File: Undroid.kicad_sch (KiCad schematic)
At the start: 43 parts, among them J1 AudioJack2, J2 Conn_01x15

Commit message: pcb-master: Update prototype.
Signed-off-by: Amlal EL Mahrouss <amlalelmahrouss@icloud.com>
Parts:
- removed AE1: Antenna_Shield, RF_Antenna:Texas_SWRA117D_2.4GHz_Right, symbol Device:Antenna_Shield
- removed ANT_S1, SD_S1, SIM_S1, USB_S1: RFShield_OnePiece, RF_Shielding:Laird_Technologies_97-2002_25.40x25.40mm, symbol Device:RFShield_OnePiece
- added ANT1: Antenna, RF_Antenna:NiceRF_SW868-TH13_868Mhz, symbol Device:Antenna
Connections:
- net at SIM_CHIP1.32 (ANT): now also ANT1.1 (A)
- no-connect marks 114 -> 117

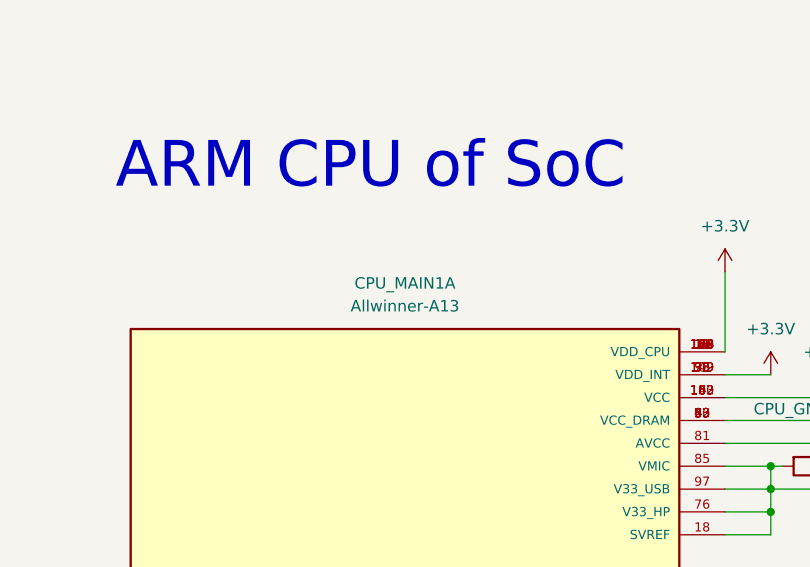
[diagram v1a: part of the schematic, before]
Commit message: pcb-master: Fix schematic and PCB.
Signed-off-by: Amlal EL Mahrouss <amlalelmahrouss@icloud.com>
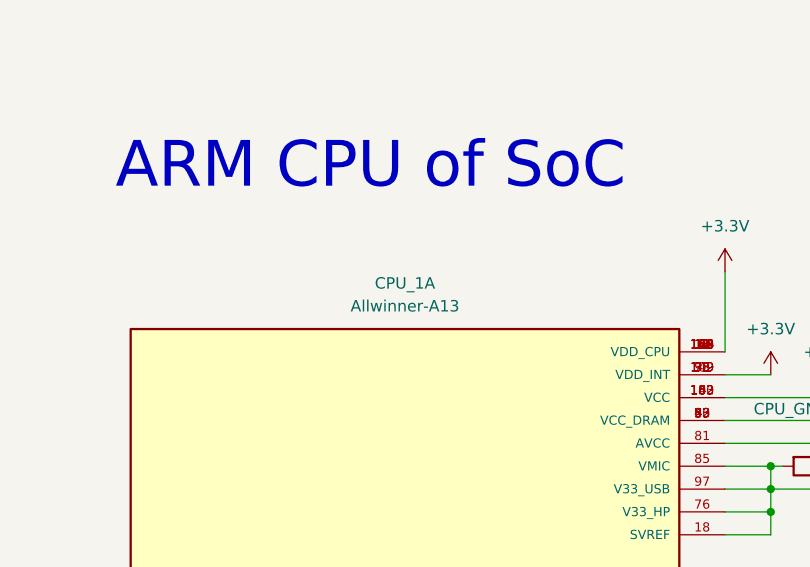
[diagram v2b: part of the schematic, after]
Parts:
- renumbered CPU_MAIN1 to CPU_1
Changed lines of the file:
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@@
 		(dnp no)
 		(fields_autoplaced yes)
-		(property "Reference" "CPU_MAIN1"
+		(property "Reference" "CPU_1"
 			(at 508 81.28 0)
 			(effects
@@
 			(project "Undroid"
 				(path "/5d3a3bfa-72d2-42b8-bac3-6ac6fe44d852"
-					(reference "CPU_MAIN1")
+					(reference "CPU_1")
 					(unit 1)
 				)

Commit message: pcb-master: update schematic.
Signed-off-by: Amlal EL Mahrouss <amlalelmahrouss@icloud.com>
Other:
- note added: "CONN 1x15"
- note removed: "The board also contains EMI shields. for Antennas, SIM, SD, Power..."
- moved on the sheet: J2
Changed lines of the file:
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@@
 	(title_block
 		(title "Motherboard")
-		(date "2024-06-17")
-		(rev "8")
+		(date "2024-06-19")
+		(rev "9")
 		(company "Zeta")
 	)
@@
 	)
 	(no_connect
-		(at 304.8 377.19)
+		(at 242.57 356.87)
 	)
 	(no_connect
@@
 	)
 	(no_connect
-		(at 307.34 377.19)
+		(at 245.11 356.87)
 	)
 	(no_connect
@@
 	)
 	(no_connect
-		(at 312.42 377.19)
+		(at 250.19 356.87)
 	)
 	(no_connect
@@
 	)
 	(no_connect
-		(at 325.12 377.19)
+		(at 262.89 356.87)
 	)
 	(no_connect
@@
 	)
 	(no_connect
-		(at 309.88 377.19)
+		(at 247.65 356.87)
 	)
 	(no_connect
-		(at 327.66 377.19)
+		(at 265.43 356.87)
 	)
 	(no_connect
@@
 	)
 	(no_connect
-		(at 314.96 377.19)
+		(at 252.73 356.87)
 	)
 	(no_connect
@@
 	)
 	(no_connect
-		(at 317.5 377.19)
+		(at 255.27 356.87)
 	)
 	(no_connect
@@
 	)
 	(no_connect
-		(at 322.58 377.19)
+		(at 260.35 356.87)
 	)
 	(no_connect
@@
 	)
 	(no_connect
-		(at 330.2 377.19)
+		(at 267.97 356.87)
 	)
 	(no_connect
@@
 	)
 	(no_connect
-		(at 320.04 377.19)
+		(at 257.81 356.87)
 	)
 	(wire
@@
 		)
 	)
-	(text "The board also contains EMI shields.\nfor Antennas, SIM, SD, Power..."
+	(text "Bridge MCU"
 		(exclude_from_sim yes)
-		(at 92.456 383.286 0)
+		(at 295.402 66.294 0)
 		(effects
 			(font
@@
 		)
 	)
-	(text "Bridge MCU"
+	(text "Memory (SIM, Flash, SD)"
 		(exclude_from_sim yes)
-		(at 295.402 66.294 0)
+		(at 105.156 326.898 0)
 		(effects
 			(font
@@
 		)
 	)
-	(text "Memory (SIM, Flash, SD)"
+	(text "ARM GPU of SoC"
 		(exclude_from_sim yes)
-		(at 79.248 317.754 0)
+		(at 505.206 242.824 0)
 		(effects
 			(font
@@
 		)
 	)
-	(text "ARM GPU of SoC"
+	(text "ARM CPU of SoC"
 		(exclude_from_sim yes)
-		(at 493.522 243.078 0)
+		(at 509.778 61.468 0)
 		(effects
 			(font
@@
 		)
 	)
-	(text "ARM CPU of SoC"
+	(text "Power Line"
 		(exclude_from_sim yes)
-		(at 504.19 68.326 0)
+		(at 177.8 178.054 0)
 		(effects
 			(font
@@
 		)
 	)
-	(text "Power Line"
+	(text "CONN 1x15"
 		(exclude_from_sim yes)
-		(at 212.09 124.968 0)
+		(at 259.842 332.486 0)
 		(effects
 			(font
@@
 	(text "GPRS modem"
 		(exclude_from_sim yes)
-		(at 80.01 47.498 0)
+		(at 73.152 53.848 0)
 		(effects
 			(font
@@
 	(global_label "CONN_NMI_N"
 		(shape input)
-		(at 332.74 377.19 90)
+		(at 270.51 356.87 90)
 		(fields_autoplaced yes)
 		(effects
@@
 		)
 		(property "Intersheetrefs" "${INTERSHEET_REFS}"
-			(at 332.74 362.2909 90)
+			(at 270.51 341.9709 90)
 			(effects
 				(font
@@
 	(global_label "RESET"
 		(shape input)
-		(at 337.82 377.19 90)
+		(at 275.59 356.87 90)
 		(fields_autoplaced yes)
 		(effects
@@
 		)
 		(property "Intersheetrefs" "${INTERSHEET_REFS}"
-			(at 337.82 368.4597 90)
+			(at 275.59 348.1397 90)
 			(effects
 				(font
@@
 	(global_label "RTC_IN"
 		(shape input)
-		(at 335.28 377.19 90)
+		(at 273.05 356.87 90)
 		(fields_autoplaced yes)
 		(effects
@@
 		)
 		(property "Intersheetrefs" "${INTERSHEET_REFS}"
-			(at 335.28 367.7943 90)
+			(at 273.05 347.4743 90)
 			(effects
 				(font
@@
 	(global_label "UBOOT"
 		(shape input)
-		(at 340.36 377.19 90)
+		(at 278.13 356.87 90)
 		(fields_autoplaced yes)
 		(effects
@@
 		)
 		(property "Intersheetrefs" "${INTERSHEET_REFS}"
-			(at 340.36 367.9757 90)
+			(at 278.13 347.6557 90)
 			(effects
 				(font
@@
 	(symbol
 		(lib_id "Connector_Generic:Conn_01x15")
-		(at 322.58 382.27 270)
+		(at 260.35 361.95 270)
 		(unit 1)
 		(exclude_from_sim no)
@@
 		(fields_autoplaced yes)
 		(property "Reference" "J2"
-			(at 322.58 386.08 90)
+			(at 260.35 365.76 90)
 			(effects
 				(font
@@
 		)
 		(property "Value" "Conn_01x15"
-			(at 322.58 388.62 90)
+			(at 260.35 368.3 90)
 			(effects
 				(font
@@
 		)
 		(property "Footprint" "Connector_PinHeader_1.00mm:PinHeader_1x15_P1.00mm_Vertical"
-			(at 322.58 382.27 0)
+			(at 260.35 361.95 0)
 			(effects
 				(font
@@
 		)
 		(property "Datasheet" "~"
-			(at 322.58 382.27 0)
+			(at 260.35 361.95 0)
 			(effects
 				(font
@@
 		)
 		(property "Description" "Generic connector, single row, 01x15, script generated (kicad-library-utils/schlib/autogen/connector/)"
-			(at 322.58 382.27 0)
+			(at 260.35 361.95 0)
 			(effects
 				(font

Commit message: pcb-master: improve schematics to be much more organized.
Signed-off-by: Amlal EL Mahrouss <amlalelmahrouss@icloud.com>
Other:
- title: Motherboard -> Phone motherboard
- moved on the sheet: ANT1, BRIDGE_CHIP1, CC1_R1, CC2_R1, CPU_1A, CPU_GND_CPU1, CPU_GND_USB1, CPU_GND_VDDQ1, CPU_GND_VREFCA1, CPU_GND_VREFQ1, D1, DDR_RAM1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

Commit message: pcb-master: improve schematic and PCB.
Signed-off-by: Amlal EL Mahrouss <amlalelmahrouss@icloud.com>
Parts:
- removed CPU_GND_USB1, CPU_GND_VDDQ1, CPU_GND_VREFCA1, CPU_GND_VREFQ1, RCPU_GND_VDD1: R, Resistor_SMD:R_0201_0603Metric, symbol Device:R
- added C1: C_Polarized, Capacitor_Tantalum_SMD:CP_EIA-2012-12_Kemet-R, symbol Device:C_Polarized
- added MBCI_0: AVR32DB32x-xRXB, Package_DFN_QFN:QFN-32-1EP_5x5mm_P0.5mm_EP3.1x3.1mm, symbol MCU_Microchip_AVR_Dx:AVR32DB32x-xRXB
- added MBCI_NETWORK1, MBCI_VIDEO1: Conn_01x15, Connector_PinHeader_1.00mm:PinHeader_1x15_P1.00mm_Vertical, symbol Connector_Generic:Conn_01x15
- added MBCI_PWR_R1, MCU_PWR_R2, RAM_GND_VSS_R3, RAM_PWR_R2: R, Resistor_SMD:R_0201_0603Metric, symbol Device:R
- renumbered CPU_GND_CPU1 to CPU_GND_1, J1 to JACK_PORT1, J2 to MBCI_IO1, RVCC_FL_2 to VCC_FL_2, RVCC_S_1 to VCC_S_1
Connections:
- net GND: now also MBCI_IO1.15 (Pin_15), MBCI_NETWORK1.15 (Pin_15), MBCI_VIDEO1.15 (Pin_15), RAM_GND_VSS_R3.1
- net RESET: now also MBCI_0.26 (~{RESET}/PF6)
- net VBUS_USBC: now also MCU_PWR_R1.2, R_VDD_3V3.1, VBAT_R1.1, MBCI_PWR_R1.2, MCU_PWR_R2.2
- net CLK: now reaches MBCI_IO1.11 (Pin_11)
- net CLK: now also MBCI_NETWORK1.11 (Pin_11), MBCI_VIDEO1.11 (Pin_11)
- net UBOOT_MBCI: now reaches MBCI_IO1.5 (Pin_5)
- net UBOOT_MBCI: now also MBCI_0.27 (UPDI)
- net 3.3V: now reaches MBCI_IO1.8 (Pin_8)
- net 3.3V: now also MBCI_NETWORK1.8 (Pin_8), MBCI_VIDEO1.8 (Pin_8)
- net at DDR_RAM1.B2 (VDD), DDR_RAM1.D9 (VDD), DDR_RAM1.G7 (VDD)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: now also RAM_PWR_R2.1
- removed net +3.3V: CPU_1.100 (VCC), CPU_1.109 (VDD_INT), CPU_1.11 (VDD_CPU), CPU_1.142 (VCC), CPU_1.149 (VDD_INT), CPU_1.156 (VDD_CPU), CPU_1.16 (VDD_CPU), CPU_1.163 (VCC), CPU_1.164 (VDD_CPU), CPU_1.169 (VDD_CPU), CPU_1.173 (VDD_CPU), CPU_1.23 (VCC_DRAM), CPU_1.30 (VCC_DRAM), CPU_1.35 (VDD_INT), CPU_1.4 (VDD_CPU), CPU_1.43 (VCC_DRAM), CPU_1.5 (VCC), CPU_1.53 (VCC_DRAM), CPU_1.62 (VCC_DRAM), CPU_1.73 (VDD_INT), CPU_1.81 (AVCC), CPU_1.9 (VDD_CPU), CPU_1.98 (VDD_INT), MCU_PWR_R1.2, R_VDD_3V3.1, VBAT_R1.1
- new net: CPU_1.109 (VDD_INT), CPU_1.149 (VDD_INT), CPU_1.35 (VDD_INT), CPU_1.73 (VDD_INT), CPU_1.98 (VDD_INT)
- new net: CPU_1.11 (VDD_CPU), CPU_1.156 (VDD_CPU), CPU_1.16 (VDD_CPU), CPU_1.164 (VDD_CPU), CPU_1.169 (VDD_CPU), CPU_1.173 (VDD_CPU), CPU_1.4 (VDD_CPU), CPU_1.9 (VDD_CPU)
- new net: C1.1, MBCI_0.28 (VDD), MBCI_PWR_R1.1
- new net: C1.2, MBCI_0.29 (GND), MBCI_0.33 (GND), RAM_GND_VSS_R3.2
- new net ALPHA_V: MBCI_0.9 (PC3), MBCI_VIDEO1.4 (Pin_4)
- new net AVAIL_N: MBCI_0.30 (XTALHF1/PA0), MBCI_NETWORK1.6 (Pin_6)
- new net BLUE_V: MBCI_0.22 (PF2), MBCI_VIDEO1.3 (Pin_3)
- new net CPU_PWR: CPU_1.100 (VCC), CPU_1.142 (VCC), CPU_1.163 (VCC), CPU_1.5 (VCC), MCU_PWR_R2.1
- new net DAT0_N: MBCI_0.3 (PA5), MBCI_NETWORK1.1 (Pin_1)
- new net DAT1_N: MBCI_0.2 (PA4), MBCI_NETWORK1.2 (Pin_2)
- new net DAT2_N: MBCI_0.1 (PA3), MBCI_NETWORK1.3 (Pin_3)
- new net DAT3_N: MBCI_0.32 (PA2), MBCI_NETWORK1.4 (Pin_4)
- new net DAT4_N: MBCI_0.31 (XTALHF2/PA1), MBCI_NETWORK1.5 (Pin_5)
- new net DRAM_PWR: CPU_1.23 (VCC_DRAM), CPU_1.30 (VCC_DRAM), CPU_1.43 (VCC_DRAM), CPU_1.53 (VCC_DRAM), CPU_1.62 (VCC_DRAM), RAM_PWR_R2.2
- new net GREEN_V: MBCI_0.21 (XTAL32K2/PF1), MBCI_VIDEO1.2 (Pin_2)
- new net HSYNC_V: MBCI_0.8 (PC2), MBCI_VIDEO1.5 (Pin_5)
- new net RED_V: MBCI_0.20 (XTAL32K1/PF0), MBCI_VIDEO1.1 (Pin_1)
- new net VSYNC_V: MBCI_0.7 (PC1), MBCI_VIDEO1.6 (Pin_6)
- now unconnected: CPU_1.18 (SVREF), CPU_1.76 (V33_HP), CPU_1.85 (VMIC), CPU_1.97 (V33_USB)
- no-connect marks 117 -> 151
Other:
- note added: "Bridge MCU+Jack"
- note added: "Bridge Power CPU Power"
- note added: "GPRS Modem"
- note added: "Iteration 2 will have MBCI support"
- note added: "Jack"
- note added: "MBCI IO"
- note added: "MBCI NET"
- note added: "MBCI VIDEO"
- note added: "MBCI controller is a read only chip and writes to Bridge."
- note added: "MBCI doesnt write here directly."
- note added: "MBCI_CTRL"
- note removed: "Bridge MCU"
- note removed: "Bridge Power"
- note removed: "CONN 1x15"
- note removed: "GPRS modem"
- moved on the sheet: ANT1, JACK_PORT1, MCU_PWR_R1, R_AUDIO1

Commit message: update sch.
Signed-off-by: Amlal El Mahrouss <amlal.elmahrouss@icloud.com>
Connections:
- net PWR_TST: no longer names the net of BRIDGE_CHIP1.37 (TST)
- no-connect marks 151 -> 152
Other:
- note added: "All of them are NC"
- note added: "Bridge MCU"
- note added: "MicroChip Need the IDE for BridgeOS"
- note removed: "Bridge MCU+Jack"
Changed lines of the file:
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@@
 	)
 	(junction
-		(at 219.71 142.24)
-		(diameter 0)
-		(color 0 0 0 0)
-	)
-	(junction
 		(at 129.54 346.71)
 		(diameter 0)
@@
 	)
 	(no_connect
+		(at 227.33 142.24)
+	)
+	(no_connect
 		(at 414.02 97.79)
 	)
@@
 	(wire
 		(pts
-			(xy 219.71 138.43) (xy 219.71 142.24)
-		)
-		(stroke
-			(width 0)
-			(type default)
-		)
-	)
-	(wire
-		(pts
 			(xy 326.39 358.14) (xy 347.98 358.14)
 		)
@@
 	(wire
 		(pts
-			(xy 213.36 142.24) (xy 219.71 142.24)
-		)
-		(stroke
-			(width 0)
-			(type default)
-		)
-	)
-	(wire
-		(pts
 			(xy 158.75 322.58) (xy 152.4 322.58)
 		)
@@
 	(wire
 		(pts
-			(xy 219.71 142.24) (xy 227.33 142.24)
-		)
-		(stroke
-			(width 0)
-			(type default)
-		)
-	)
-	(wire
-		(pts
 			(xy 407.67 340.36) (xy 407.67 363.22)
 		)
@@
 		)
 	)
-	(text "Bridge MCU+Jack"
+	(text "Bridge MCU"
 		(exclude_from_sim yes)
 		(at 251.206 30.48 0)
@@
 		)
 	)
+	(text "MicroChip\nNeed the IDE\nfor BridgeOS"
+		(exclude_from_sim yes)
+		(at 199.136 44.45 0)
+		(effects
+			(font
+				(size 5.08 5.08)
+			)
+		)
+	)
+	(text "All of them are NC"
+		(exclude_from_sim yes)
+		(at 372.618 43.434 0)
+		(effects
+			(font
+				(size 5.08 5.08)
+			)
+		)
+	)
 	(text "MBCI VIDEO"
 		(exclude_from_sim yes)
@@
 		)
 	)
-	(global_label "PWR_TST"
-		(shape input)
-		(at 213.36 142.24 180)
-		(fields_autoplaced yes)
-		(effects
-			(font
-				(size 1.27 1.27)
-			)
-			(justify right)
-		)
-		(property "Intersheetrefs" "${INTERSHEET_REFS}"
-			(at 202.2711 142.24 0)
-			(effects
-				(font
-					(size 1.27 1.27)
-				)
-				(justify right)
-				(hide yes)
-			)
-		)
-	)
 	(global_label "A10{slash}AP"
 		(shape input)
@@
 					(unit 1)
 				)
-			)
-		)
-	)
-	(symbol
-		(lib_id "power:PWR_FLAG")
-		(at 219.71 138.43 0)
-		(unit 1)
-		(exclude_from_sim no)
-		(in_bom yes)
-		(on_board yes)
-		(dnp no)
-		(fields_autoplaced yes)
-		(property "Reference" "#FLG017"
-			(at 219.71 136.525 0)
-			(effects
-				(font
-					(size 1.27 1.27)
-				)
-				(hide yes)
-			)
-		)
-		(property "Value" "PWR_FLAG"
-			(at 219.71 133.35 0)
-			(effects
-				(font
-					(size 1.27 1.27)
-				)
-			)
-		)
-		(property "Footprint" ""
-			(at 219.71 138.43 0)
-			(effects
-				(font
-					(size 1.27 1.27)
-				)
-				(hide yes)
-			)
-		)
-		(property "Datasheet" "~"
-			(at 219.71 138.43 0)
-			(effects
-				(font
-					(size 1.27 1.27)
-				)
-				(hide yes)
-			)
-		)
-		(property "Description" "Special symbol for telling ERC where power comes from"
-			(at 219.71 138.43 0)
-			(effects
-				(font
-					(size 1.27 1.27)
-				)
-				(hide yes)
-			)
-		)
-		(pin "1"
-		)
-		(instances
-			(project "Undroid"
-				(path "/5d3a3bfa-72d2-42b8-bac3-6ac6fe44d852"
-					(reference "#FLG017")
-					(unit 1)
-				)

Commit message: Undroid: Fix schematic.
Signed-off-by: Amlal El Mahrouss <amlal.elmahrouss@icloud.com>
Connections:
- net A11: now also MBCI_0.11 (PD1)
- net A12/BC_N: now also MBCI_0.12 (PD2); no longer BRIDGE_CHIP1.20 (PD25)
- net A13: now also MBCI_0.13 (PD3); no longer BRIDGE_CHIP1.21 (PD26)
- net A14: now also MBCI_0.14 (PD4); no longer BRIDGE_CHIP1.2 (PD31)
- net RAM_BA0: now also BRIDGE_CHIP1.20 (PD25), MBCI_0.17 (VREFA/PD7)
- net RAM_BA1: now also BRIDGE_CHIP1.21 (PD26), MBCI_0.16 (PD6)
- net RAM_BA2: now also BRIDGE_CHIP1.2 (PD31), MBCI_0.15 (PD5)
- net RX2: no longer names the net of BRIDGE_CHIP1.47 (PB5)
- net TX2: no longer names the net of BRIDGE_CHIP1.46 (PB4)
- no-connect marks 152 -> 147
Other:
- note added: "All of them are NC for now we dont use the GPU"
- note added: "MBCI controller is DMA only"
- note removed: "All of them are NC"
- note removed: "MBCI controller is a read only chip and writes to Bridge."
- note removed: "MBCI doesnt write here directly."
- note removed: "MicroChip Need the IDE for BridgeOS"
- moved on the sheet: RAM_PWR_R2

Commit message: board: major improvements.
Signed-off-by: Amlal EL Mahrouss <amlalelmahrouss@icloud.com>
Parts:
- removed GPU_1: Allwinner-A13, QFP40P2200X2200X160-177N, symbol Allwinner:Allwinner-A13
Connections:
- no-connect marks 147 -> 71
